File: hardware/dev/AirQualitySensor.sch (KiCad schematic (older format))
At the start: 44 parts, among them J1 USB_C_Receptacle_USB2.0, J2 SWD, J3 UART, U1 004-0-0053, U2 DHT22, U3 XC6206P332MR

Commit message: Fix inductor footprint
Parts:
- FB1, FB2: footprint Inductor_SMD:L_0805_2012Metric -> Inductor_SMD:L_0805_2012Metric_Pad1.15x1.40mm_HandSolder
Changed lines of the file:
@@
 F 0 "FB2" V 2613 1500 50  0000 C CNN
 F 1 "100R" V 2704 1500 50  0000 C CNN
-F 2 "Inductor_SMD:L_0805_2012Metric" V 2780 1500 50  0001 C CNN
+F 2 "Inductor_SMD:L_0805_2012Metric_Pad1.15x1.40mm_HandSolder" V 2780 1500 50  0001 C CNN
 F 3 "~" H 2850 1500 50  0001 C CNN
 F 4 "GZ2012D101TF" H 2850 1500 50  0001 C CNN "Description"
@@
 F 0 "FB1" V 2613 1050 50  0000 C CNN
 F 1 "100R" V 2704 1050 50  0000 C CNN
-F 2 "Inductor_SMD:L_0805_2012Metric" V 2780 1050 50  0001 C CNN
+F 2 "Inductor_SMD:L_0805_2012Metric_Pad1.15x1.40mm_HandSolder" V 2780 1050 50  0001 C CNN
 F 3 "~" H 2850 1050 50  0001 C CNN
 F 4 "GZ2012D101TF" H 2850 1050 50  0001 C CNN "Description"

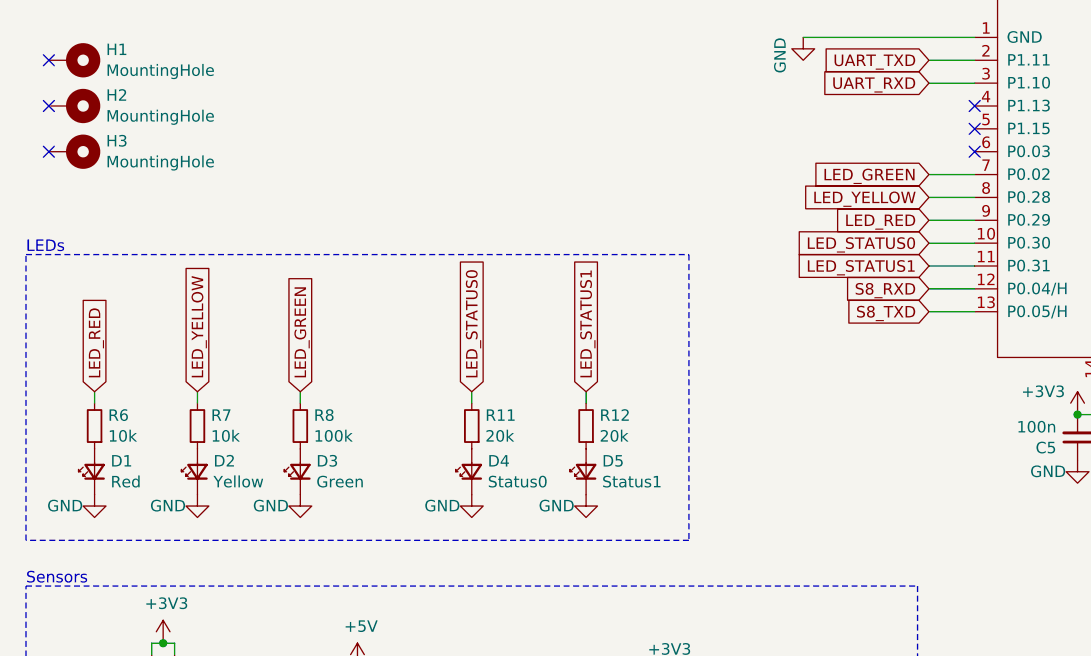
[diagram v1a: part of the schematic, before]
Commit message: Fix flipped red-green LEDs
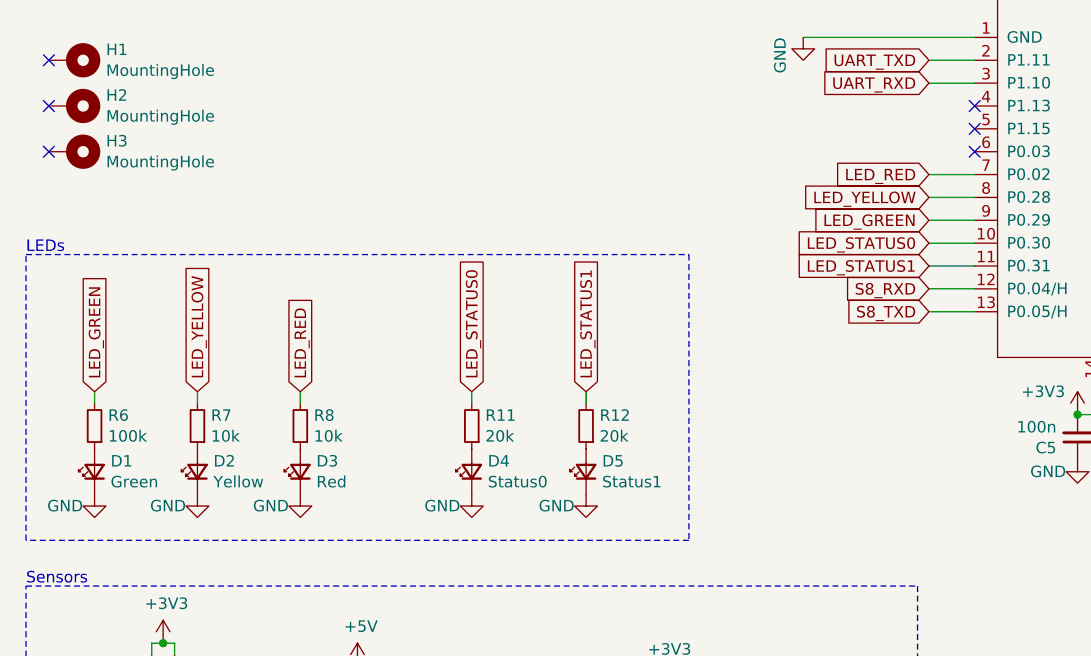
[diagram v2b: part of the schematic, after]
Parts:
- D1: value Red -> Green
- D3: value Green -> Red
- R6: value 10k -> 100k
- R8: value 100k -> 10k
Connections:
- net LED_GREEN: now also A1.9 (P0.29), R6.2; no longer A1.7 (P0.02), R8.2
- net LED_RED: now also A1.7 (P0.02), R8.2; no longer A1.9 (P0.29), R6.2
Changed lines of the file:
@@
 P 1050 5600
 F 0 "D1" V 1096 5530 50  0000 R CNN
-F 1 "Red" V 1005 5530 50  0000 R CNN
+F 1 "Green" V 1005 5530 50  0000 R CNN
 F 2 "LED_THT:LED_D3.0mm" V 1050 5600 50  0001 C CNN
 F 3 "~" V 1050 5600 50  0001 C CNN
@@
 P 1950 5600
 F 0 "D3" V 1996 5530 50  0000 R CNN
-F 1 "Green" V 1905 5530 50  0000 R CNN
+F 1 "Red" V 1905 5530 50  0000 R CNN
 F 2 "LED_THT:LED_D3.0mm" V 1950 5600 50  0001 C CNN
 F 3 "~" V 1950 5600 50  0001 C CNN
@@
 P 1950 5400
 F 0 "R8" H 1891 5354 50  0000 R CNN
-F 1 "100k" H 1891 5445 50  0000 R CNN
+F 1 "10k" H 1891 5445 50  0000 R CNN
 F 2 "Resistor_SMD:R_0402_1005Metric" H 1950 5400 50  0001 C CNN
 F 3 "~" H 1950 5400 50  0001 C CNN
@@
 P 1050 5400
 F 0 "R6" H 991 5354 50  0000 R CNN
-F 1 "10k" H 991 5445 50  0000 R CNN
+F 1 "100k" H 991 5445 50  0000 R CNN
 F 2 "Resistor_SMD:R_0402_1005Metric" H 1050 5400 50  0001 C CNN
 F 3 "~" H 1050 5400 50  0001 C CNN
@@
 $EndComp
 Text GLabel 1050 5250 1    50   Input ~ 0
-LED_RED
+LED_GREEN
 Text GLabel 1500 5250 1    50   Input ~ 0
 LED_YELLOW
 Text GLabel 1950 5250 1    50   Input ~ 0
-LED_GREEN
+LED_RED
 Wire Wire Line
 	1950 5250 1950 5300
@@
 NoConn ~ 5550 5200
 Text GLabel 4700 4300 0    50   Input ~ 0
+LED_RED
+Text GLabel 4700 4500 0    50   Input ~ 0
 LED_GREEN
-Text GLabel 4700 4500 0    50   Input ~ 0
-LED_RED
 Wire Wire Line
 	2150 1050 2600 1050
